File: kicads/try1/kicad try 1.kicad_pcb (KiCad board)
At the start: 2 copper layers, 4 parts

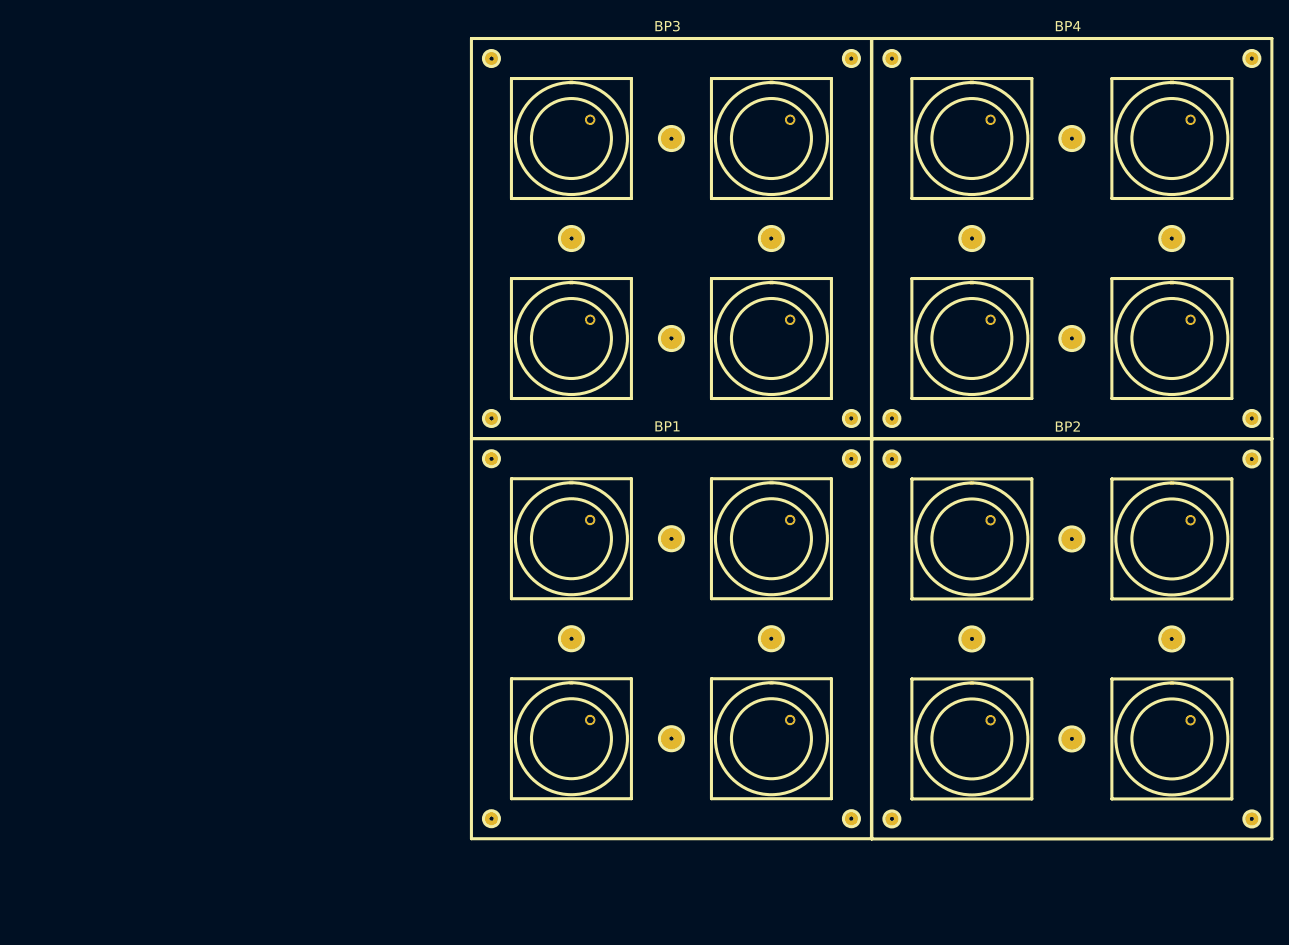
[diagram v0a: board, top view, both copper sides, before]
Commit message: figured out how to make button pads wiring and library files, going forward with the electronic schematic
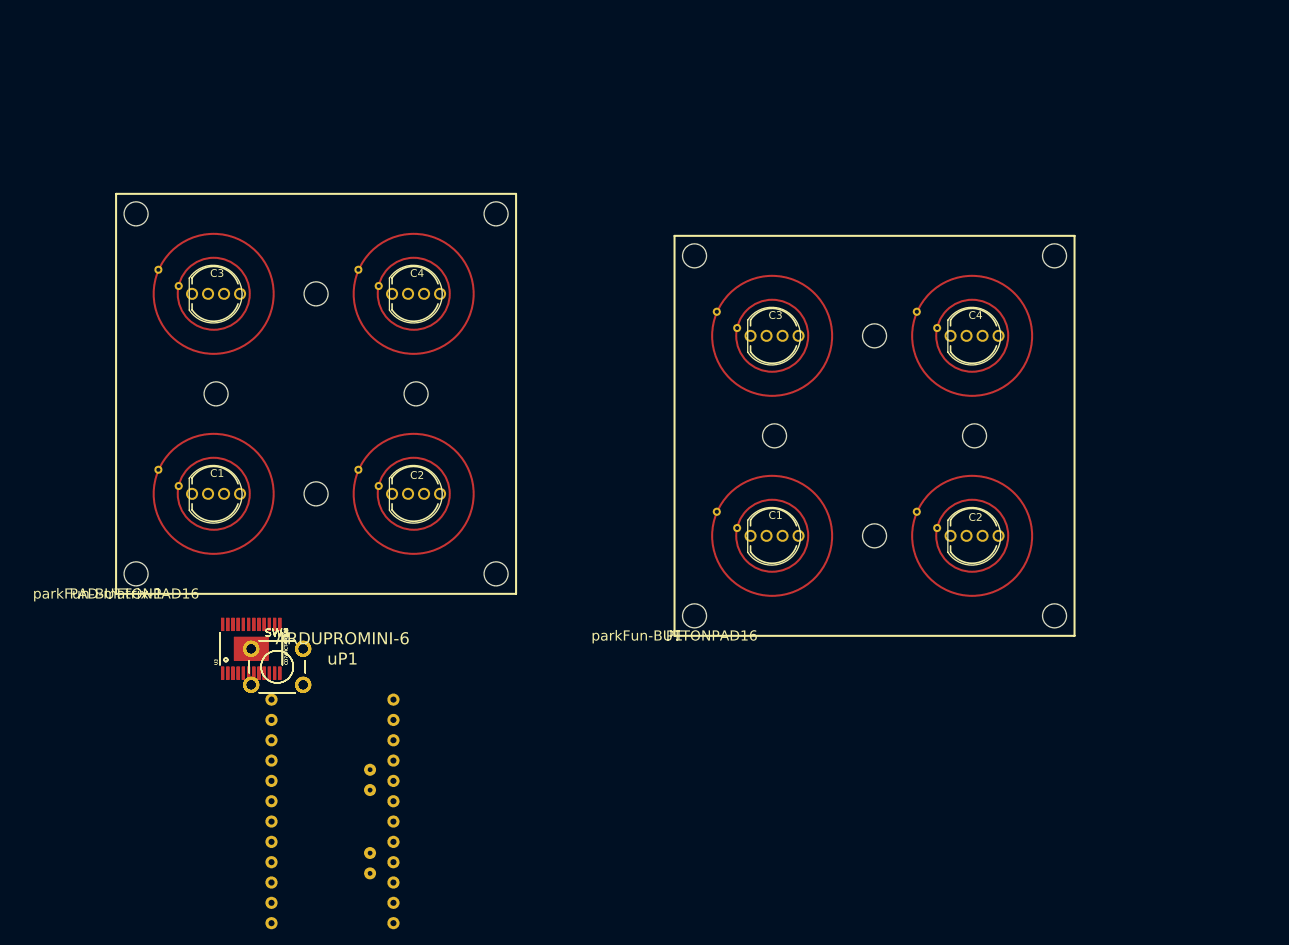
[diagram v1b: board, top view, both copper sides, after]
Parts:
- removed BP1, BP2, BP3, BP4: button_pad_silicon_2X2_GBRA, button_pad_silicon_2x2:button_pad_silicon_2x2
- added P1: parkFun-BUTTONPAD16, button-pad-autotel:2x2-buttonpad-sparkfun-autotel, F.Cu at (201.4, 103.4)
- added PAD-matrix-1: parkFun-BUTTONPAD16, button-pad-autotel:2x2-buttonpad-sparkfun-autotel, F.Cu at (131.6, 98.1)
- added SW1, SW3, SW4, SW5: SW_PUSH, Buttons_Switches_ThroughHole:SW_PUSH_6mm, F.Cu at (148.5, 105.0)
- added U2, U3: CD74HCT4067, SparkFun-DigitalIC:TSSOP-24, F.Cu at (148.5, 105.0)
- added uP1: ARDUPROMINI-6, ArduProMiniTKB:ArduProMini-6, F.Cu at (148.5, 105.0)
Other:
- rule pad_to_mask_clearance: 0.2 -> 0

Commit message: FIX 16*4 pads error
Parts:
- removed SW5: SW_PUSH, Buttons_Switches_ThroughHole:SW_PUSH_6mm
- added D1: D, Diodes_ThroughHole:Diode_DO-41_SOD81_Horizontal_RM10, F.Cu at (105.5, 96.1)
- added D10: D, Diodes_ThroughHole:Diode_DO-41_SOD81_Horizontal_RM10, F.Cu at (152.7, 84.6)
- added D11: D, Diodes_ThroughHole:Diode_DO-41_SOD81_Horizontal_RM10, F.Cu at (160.4, 97.9)
- added D12: D, Diodes_ThroughHole:Diode_DO-41_SOD81_Horizontal_RM10, F.Cu at (144.5, 76.5)
- added D13: D, Diodes_ThroughHole:Diode_DO-41_SOD81_Horizontal_RM10, F.Cu at (160.3, 82.0)
- added D14: D, Diodes_ThroughHole:Diode_DO-41_SOD81_Horizontal_RM10, F.Cu at (137.5, 71.5)
- added D15: D, Diodes_ThroughHole:Diode_DO-41_SOD81_Horizontal_RM10, F.Cu at (169.7, 88.6)
- added D16: D, Diodes_ThroughHole:Diode_DO-41_SOD81_Horizontal_RM10, F.Cu at (178.9, 98.4)
- added D2: D, Diodes_ThroughHole:Diode_DO-41_SOD81_Horizontal_RM10, F.Cu at (185.4, 132.8)
- added D3: D, Diodes_ThroughHole:Diode_DO-41_SOD81_Horizontal_RM10, F.Cu at (117.0, 140.6)
- added D4: D, Diodes_ThroughHole:Diode_DO-41_SOD81_Horizontal_RM10, F.Cu at (159.6, 76.8)
- added D5: D, Diodes_ThroughHole:Diode_DO-41_SOD81_Horizontal_RM10, F.Cu at (186.8, 126.9)
- added D6: D, Diodes_ThroughHole:Diode_DO-41_SOD81_Horizontal_RM10, F.Cu at (151.0, 92.6)
- added D7: D, Diodes_ThroughHole:Diode_DO-41_SOD81_Horizontal_RM10, F.Cu at (138.4, 87.1)
- added D8: D, Diodes_ThroughHole:Diode_DO-41_SOD81_Horizontal_RM10, F.Cu at (142.0, 97.9)
- added D9: D, Diodes_ThroughHole:Diode_DO-41_SOD81_Horizontal_RM10, F.Cu at (150.4, 88.0)
- added P2: CONN_01X08, SparkFun-Connectors:1X08, F.Cu at (94.0, 71.9)
- added P3: CONN_01X08, SparkFun-Connectors:1X08, F.Cu at (93.2, 76.2)
- added P4: CONN_01X08, SparkFun-Connectors:1X08, F.Cu at (93.9, 84.3)
- added P5: CONN_01X08, SparkFun-Connectors:1X08, F.Cu at (93.0, 79.6)
- added P6: CONN_01X08, SparkFun-Connectors:1X08, F.Cu at (113.2, 82.3)
- added PAD-matrix-10: BP7, button-pad-autotel:2x2-buttonpad-sparkfun-autotel, F.Cu at (205.1, 102.2)
- added PAD-matrix-2: BP15, button-pad-autotel:2x2-buttonpad-sparkfun-autotel, F.Cu at (255.0, 52.3)
- added PAD-matrix-6: BP11, button-pad-autotel:2x2-buttonpad-sparkfun-autotel, F.Cu at (205.1, 52.3)
- added R1: R, Resistors_ThroughHole:Resistor_Horizontal_RM10mm, F.Cu at (131.2, 75.3)
- added R2: R, Resistors_ThroughHole:Resistor_Horizontal_RM10mm, F.Cu at (144.5, 82.0)
- added SW2: SW_PUSH, Buttons_Switches_ThroughHole:SW_PUSH_6mm, F.Cu at (195.6, 111.7)
- P1: value parkFun-BUTTONPAD16 -> CONN_01X08; footprint button-pad-autotel:2x2-buttonpad-sparkfun-autotel -> SparkFun-Connectors:1X08
- PAD-matrix-1: value parkFun-BUTTONPAD16 -> BP3
- moved PAD-matrix-1 123.5 mm to (255.1, 102.2)
- moved P1 98.7 mm to (104.3, 120.8)
- moved uP1 94.7 mm to (58.4, 75.9)
- moved SW3 50.8 mm to (197.0, 120.2)
- moved U3 39.8 mm to (178.5, 78.9)
- moved U2 39.7 mm to (155.6, 65.9)
- moved SW4 39.6 mm to (185.1, 120.1)
- moved SW1 35.9 mm to (183.8, 111.5)
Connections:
- net Net-(U3-Pad16) renamed /MUX15
- net Net-(U3-Pad17) renamed /MUX14
- net Net-(U3-Pad18) renamed /MUX13
- net Net-(U3-Pad19) renamed /MUX12
- PAD-matrix-1 pad BLU1: (no net) -> /MUXAB7
- PAD-matrix-1 pad BLU2: (no net) -> /MUXAB6
- PAD-matrix-1 pad BLU3: (no net) -> /MUXAB5
- PAD-matrix-1 pad BLU4: (no net) -> /MUXAB4
- PAD-matrix-1 pad GND1: (no net) -> /MUXBG11
- PAD-matrix-1 pad GND2: (no net) -> /MUXBG11
- PAD-matrix-1 pad GND3: (no net) -> /MUXBG11
- PAD-matrix-1 pad GND4: (no net) -> /MUXBG11
- PAD-matrix-1 pad GRN1: (no net) -> /MUXAG11
- PAD-matrix-1 pad GRN2: (no net) -> /MUXAG10
- PAD-matrix-1 pad GRN3: (no net) -> /MUXAG9
- PAD-matrix-1 pad GRN4: (no net) -> /MUXAG8
- PAD-matrix-1 pad RED1: (no net) -> /MUXAR15
- PAD-matrix-1 pad RED2: (no net) -> /MUXAR14
- PAD-matrix-1 pad RED3: (no net) -> /MUXAR13
- PAD-matrix-1 pad RED4: (no net) -> /MUXAR12
- PAD-matrix-1 pad SIG1: (no net) -> /MUXAS3
- PAD-matrix-1 pad SIG2: (no net) -> Net-(D13-Pad2)
- PAD-matrix-1 pad SIG3: (no net) -> /MUXAS2
- PAD-matrix-1 pad SIG4: (no net) -> Net-(D14-Pad2)
- PAD-matrix-1 pad SIG5: (no net) -> /MUXAS1
- PAD-matrix-1 pad SIG6: (no net) -> Net-(D15-Pad2)
- PAD-matrix-1 pad SIG7: (no net) -> /MUXAS0
- PAD-matrix-1 pad SIG8: (no net) -> Net-(D16-Pad2)
- SW1 pad 1: Net-(SW1-Pad1) -> /VCC
- SW1 pad 2: Net-(SW1-Pad2) -> /MUXBS4
- SW3 pad 1: Net-(SW3-Pad1) -> /VCC
- SW3 pad 2: Net-(SW3-Pad2) -> /MUXBS6
- SW4 pad 1: Net-(SW4-Pad1) -> /VCC
- SW4 pad 2: Net-(SW4-Pad2) -> /MUXBS7
- U2 pad 1: Net-(U2-Pad1) -> /A1
- U2 pad 16: Net-(U2-Pad16) -> /MUXAR15
- U2 pad 17: Net-(U2-Pad17) -> /MUXAR14
- U2 pad 18: Net-(U2-Pad18) -> /MUXAR13
- U2 pad 19: Net-(U2-Pad19) -> /MUXAR12
- U2 pad 2: Net-(U2-Pad2) -> /MUXAB7
- U2 pad 20: Net-(U2-Pad20) -> /MUXAG11
- U2 pad 21: Net-(U2-Pad21) -> /MUXAG10
- U2 pad 22: Net-(U2-Pad22) -> /MUXAG9
- U2 pad 23: Net-(U2-Pad23) -> /MUXAG8
- U2 pad 3: Net-(U2-Pad3) -> /MUXAB6
- U2 pad 4: Net-(U2-Pad4) -> /MUXAB5
- U2 pad 5: Net-(U2-Pad5) -> /MUXAB4
- U2 pad 6: Net-(U2-Pad6) -> /MUXAS3
- U2 pad 7: Net-(PAD-matrix-1-Pad3) -> /MUXAS2
- U2 pad 8: Net-(PAD-matrix-1-Pad1) -> /MUXAS1
- U2 pad 9: Net-(PAD-matrix-1-Pad2) -> /MUXAS0
- U3 pad 10: /3(**) -> /PD4
- U3 pad 11: /2 -> /PD5
- U3 pad 13: /0(Tx) -> /PD7
- U3 pad 14: /1(Rx) -> /PD6
- U3 pad 2: Net-(U3-Pad2) -> /MUXBS7
- U3 pad 20: Net-(U3-Pad20) -> /MUXBG11
- U3 pad 21: Net-(U3-Pad21) -> /MUXBG10
- U3 pad 22: Net-(U3-Pad22) -> /MUXBG9
- U3 pad 23: Net-(U3-Pad23) -> /MUXBG8
- U3 pad 3: Net-(U3-Pad3) -> /MUXBS6
- U3 pad 4: Net-(U3-Pad4) -> /MUXBS5
- U3 pad 5: Net-(U3-Pad5) -> /MUXBS4
- U3 pad 6: Net-(U3-Pad6) -> /MUXBS3
- U3 pad 7: Net-(U3-Pad7) -> /MUXBS2
- U3 pad 8: Net-(U3-Pad8) -> /MUXBS1
- U3 pad 9: Net-(U3-Pad9) -> /MUXBS0
- uP1 pad 10: /PD3 -> GNDREF
- uP1 pad 11: Net-(uP1-Pad11) -> /PD2
- uP1 pad 12: Net-(uP1-Pad12) -> /PD3
- uP1 pad 13: Net-(uP1-Pad13) -> /PD4
- uP1 pad 14: Net-(uP1-Pad14) -> /PD5
- uP1 pad 15: Net-(uP1-Pad15) -> /PD6
- uP1 pad 16: Net-(uP1-Pad16) -> /PD7
- uP1 pad 17: Net-(uP1-Pad17) -> /PB0
- uP1 pad 18: Net-(uP1-Pad18) -> /PB1
- uP1 pad 22: Net-(uP1-Pad22) -> /VCC
- uP1 pad 23: Net-(uP1-Pad23) -> /A3
- uP1 pad 24: Net-(uP1-Pad24) -> /A2
- uP1 pad 25: Net-(uP1-Pad25) -> /A1
- uP1 pad 26: Net-(uP1-Pad26) -> /A0
- uP1 pad 27: Net-(uP1-Pad27) -> /PB5
- uP1 pad 28: Net-(uP1-Pad28) -> /PB4
- uP1 pad 29: Net-(uP1-Pad29) -> /PB3
- uP1 pad 30: Net-(uP1-Pad30) -> /PB2
- uP1 pad 31: (no net) -> /A5
- uP1 pad 32: (no net) -> /A4
- uP1 pad 34: (no net) -> /A7
- uP1 pad 35: (no net) -> /A6
- uP1 pad 9: /PD2 -> Net-(uP1-Pad9)

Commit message: corrected vertical for groups of four pads mistake
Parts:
- removed P1: CONN_01X08, SparkFun-Connectors:1X08
- removed PAD-matrix-10: BP7, button-pad-autotel:2x2-buttonpad-sparkfun-autotel
- removed PAD-matrix-6: BP11, button-pad-autotel:2x2-buttonpad-sparkfun-autotel
- added PAD-matrix-3: BP11, button-pad-autotel:2x2-buttonpad-sparkfun-autotel, F.Cu at (161.0, 153.7)
- added PAD-matrix-4: BP7, button-pad-autotel:2x2-buttonpad-sparkfun-autotel, F.Cu at (161.0, 102.9)
- added VCC: CONN_01X08, SparkFun-Connectors:1X08, F.Cu at (217.2, 71.1)
- P2: value CONN_01X08 -> GND
- P4: value CONN_01X08 -> A2 A3 A4 A5 A6
- P5: value CONN_01X08 -> Mutual
- moved uP1 156.3 mm to (196.1, 149.9), turned to 90 degrees
- moved PAD-matrix-1 153.7 mm to (110.2, 153.7), turned to 90 degrees
- moved PAD-matrix-2 153.3 mm to (110.4, 102.9), turned to 90 degrees
- moved U3 146.9 mm to (31.8, 71.1)
- moved U2 132.9 mm to (31.8, 114.3)
- moved P3 128.6 mm to (217.2, 110.5), turned to 180 degrees
- moved P2 124.5 mm to (217.2, 90.2), turned to 180 degrees
- moved P5 124.3 mm to (217.2, 83.8), turned to 180 degrees
- moved P4 106.1 mm to (199.4, 95.3)
- moved R1 100.8 mm to (217.7, 127.1), turned to 90 degrees
- moved D2 94.9 mm to (90.7, 128.3), turned to 180 degrees
- moved P6 86.5 mm to (199.4, 75.9), turned to 0 degrees
- moved R2 83.3 mm to (220.2, 116.9), turned to 270 degrees
- moved D5 76.0 mm to (114.8, 151.2), turned to 180 degrees
- moved D13 69.3 mm to (165.6, 151.2), turned to 180 degrees
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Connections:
- PAD-matrix-1 pad BLU3: /MUXAB5 -> /MUXAB7
- PAD-matrix-1 pad BLU4: /MUXAB4 -> /MUXAB6
- PAD-matrix-1 pad GND1: /MUXBG11 -> /MUXBG9
- PAD-matrix-1 pad GND2: /MUXBG11 -> /MUXBG9
- PAD-matrix-1 pad GND3: /MUXBG11 -> /MUXBG8
- PAD-matrix-1 pad GND4: /MUXBG11 -> /MUXBG8
- PAD-matrix-1 pad GRN3: /MUXAG9 -> /MUXAG11
- PAD-matrix-1 pad GRN4: /MUXAG8 -> /MUXAG10
- PAD-matrix-1 pad RED3: /MUXAR13 -> /MUXAR15
- PAD-matrix-1 pad RED4: /MUXAR12 -> /MUXAR14
- PAD-matrix-1 pad SIG2: Net-(D13-Pad2) -> Net-(D5-Pad2)
- PAD-matrix-1 pad SIG4: Net-(D14-Pad2) -> Net-(D6-Pad2)
- PAD-matrix-1 pad SIG5: /MUXAS1 -> /MUXAS3
- PAD-matrix-1 pad SIG6: Net-(D15-Pad2) -> Net-(D1-Pad2)
- PAD-matrix-1 pad SIG7: /MUXAS0 -> /MUXAS2
- PAD-matrix-1 pad SIG8: Net-(D16-Pad2) -> Net-(D2-Pad2)
- PAD-matrix-2 pad BLU1: /MUXAB7 -> /MUXAB5
- PAD-matrix-2 pad BLU2: /MUXAB6 -> /MUXAB4
- PAD-matrix-2 pad GND1: /MUXBG8 -> /MUXBG9
- PAD-matrix-2 pad GND2: /MUXBG8 -> /MUXBG9
- PAD-matrix-2 pad GRN1: /MUXAG11 -> /MUXAG9
- PAD-matrix-2 pad GRN2: /MUXAG10 -> /MUXAG8
- PAD-matrix-2 pad RED1: /MUXAR15 -> /MUXAR13
- PAD-matrix-2 pad RED2: /MUXAR14 -> /MUXAR12
- PAD-matrix-2 pad SIG1: /MUXAS3 -> /MUXAS1
- PAD-matrix-2 pad SIG2: Net-(D1-Pad2) -> Net-(D7-Pad2)
- PAD-matrix-2 pad SIG3: /MUXAS2 -> /MUXAS0
- PAD-matrix-2 pad SIG4: Net-(D2-Pad2) -> Net-(D8-Pad2)
